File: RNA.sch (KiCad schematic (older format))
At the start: 89 parts, among them J1 USB_B_Micro, J2 AudioJack4, J3 Conn_01x06, J4 AudioJack4, SW1 SW_SPST, SW11 SW_Push_45deg, SW12 SW_Push_45deg, SW13 SW_Push_45deg, SW14 SW_Push_45deg, SW15 SW_Push_45deg, SW16 SW_Push_45deg, SW2 SW_Push, SW21 SW_Push_45deg, SW22 SW_Push_45deg, SW23 SW_Push_45deg, SW24 SW_Push_45deg, SW25 SW_Push_45deg, SW26 SW_Push_45deg, SW31 SW_Push_45deg, SW32 SW_Push_45deg, SW33 SW_Push_45deg, SW34 SW_Push_45deg, SW35 SW_Push_45deg, SW36 SW_Push_45deg, SW41 SW_Push_45deg, SW42 SW_Push_45deg, SW43 SW_Push_45deg, SW44 SW_Push_45deg, SW45 SW_Push_45deg, SW46 SW_Push_45deg, SW47 SW_Push_45deg, SW51 SW_Push_45deg, SW52 SW_Push_45deg, SW53 SW_Push_45deg, SW54 SW_Push_45deg, SW55 SW_Push_45deg, SW56 SW_Push_45deg, SW57 SW_Push_45deg, U1 STM32F072C8Tx, U2 PRTR5V0U2X, U3 MCP1703A-3302_SOT23

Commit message: ready to alpha
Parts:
- removed R4: 39k, Resistor_SMD:R_0603_1608Metric, symbol Device:R_Small
- removed R7: 68k, Resistor_SMD:R_0603_1608Metric, symbol Device:R_Small
- added C9: C_Small, Capacitor_SMD:C_0603_1608Metric, symbol Device:C_Small
- added U5: CAT24M01W, Package_SO:SOIC-8_3.9x4.9mm_P1.27mm, symbol Memory_EEPROM:CAT24M01W
- C7: value C_Small -> 100u
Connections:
- net GND: now also C9.2, U5.2 (A1), U5.3 (A2), U5.4 (GND), U5.7 (WP)
- net SCL1: now also U5.6 (SCL)
- net SDA1: now also U5.5 (SDA)
- net SWO: now also J3.6 (Pin_6)
- net VDD: now also C9.1, U5.8 (VCC)
- no-connect marks 3 -> 2
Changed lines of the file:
@@
 Wire Wire Line
 	1850 5400 1850 5350
-NoConn ~ 8400 1150
 $Comp
 L Device:C_Small C7
@@
 P 4550 1450
 F 0 "C7" H 4642 1496 50  0000 L CNN
-F 1 "C_Small" H 4642 1405 50  0000 L CNN
+F 1 "100u" H 4642 1405 50  0000 L CNN
 F 2 "Capacitor_SMD:C_0603_1608Metric" H 4550 1450 50  0001 C CNN
 F 3 "~" H 4550 1450 50  0001 C CNN
@@
 Wire Wire Line
 	1750 5950 2300 5950
-$Comp
-L power:VBUS #PWR0107
-U 1 1 5CDEAD02
-P 9650 800
-F 0 "#PWR0107" H 9650 650 50  0001 C CNN
-F 1 "VBUS" H 9665 973 50  0000 C CNN
-F 2 "" H 9650 800 50  0001 C CNN
-F 3 "" H 9650 800 50  0001 C CNN
-	1    9650 800
-	1    0    0    -1
-$EndComp
-$Comp
-L power:GND #PWR0120
-U 1 1 5CDEAE65
-P 9650 1700
-F 0 "#PWR0120" H 9650 1450 50  0001 C CNN
-F 1 "GND" H 9655 1527 50  0000 C CNN
-F 2 "" H 9650 1700 50  0001 C CNN
-F 3 "" H 9650 1700 50  0001 C CNN
-	1    9650 1700
-	1    0    0    -1
-$EndComp
-$Comp
-L Device:R_Small R4
-U 1 1 5CDEAFCF
-P 9650 1050
-F 0 "R4" H 9709 1096 50  0000 L CNN
-F 1 "39k" H 9709 1005 50  0000 L CNN
-F 2 "Resistor_SMD:R_0603_1608Metric" H 9650 1050 50  0001 C CNN
-F 3 "~" H 9650 1050 50  0001 C CNN
-	1    9650 1050
-	1    0    0    -1
-$EndComp
-$Comp
-L Device:R_Small R7
-U 1 1 5CDEB0FC
-P 9650 1500
-F 0 "R7" H 9709 1546 50  0000 L CNN
-F 1 "68k" H 9709 1455 50  0000 L CNN
-F 2 "Resistor_SMD:R_0603_1608Metric" H 9650 1500 50  0001 C CNN
-F 3 "~" H 9650 1500 50  0001 C CNN
-	1    9650 1500
-	1    0    0    -1
-$EndComp
-Wire Wire Line
-	9650 950  9650 800
-Wire Wire Line
-	9650 1400 9650 1250
-Wire Wire Line
-	9650 1700 9650 1600
-Text GLabel 9850 1250 2    50   Output ~ 0
-VBUS_SENSE
-Wire Wire Line
-	9850 1250 9650 1250
-Connection ~ 9650 1250
-Wire Wire Line
-	9650 1250 9650 1150
 Connection ~ 4900 1750
 $Comp
@@
 F1 "RNA_Sub.sch" 50
 $EndSheet
+$Comp
+L Memory_EEPROM:CAT24M01W U5
+U 1 1 5D0A58A2
+P 10000 1350
+F 0 "U5" H 10000 1831 50  0000 C CNN
+F 1 "CAT24M01W" H 10000 1740 50  0000 C CNN
+F 2 "Package_SO:SOIC-8_3.9x4.9mm_P1.27mm" H 10850 1100 50  0001 C CNN
+F 3 "https://www.onsemi.com/pub/Collateral/CAT24M01-D.PDF" H 10000 1350 50  0001 C CNN
+	1    10000 1350
+	1    0    0    -1
+$EndComp
+Wire Wire Line
+	8650 1150 8400 1150
+$Comp
+L power:GND #PWR0107
+U 1 1 5D0C7181
+P 10000 1850
+F 0 "#PWR0107" H 10000 1600 50  0001 C CNN
+F 1 "GND" H 10005 1677 50  0000 C CNN
+F 2 "" H 10000 1850 50  0001 C CNN
+F 3 "" H 10000 1850 50  0001 C CNN
+	1    10000 1850
+	1    0    0    -1
+$EndComp
+Wire Wire Line
+	10000 1650 10000 1750
+Wire Wire Line
+	9600 1450 9600 1750
+Wire Wire Line
+	9600 1750 10000 1750
+Connection ~ 10000 1750
+Wire Wire Line
+	10000 1750 10000 1850
+Wire Wire Line
+	9600 1350 9600 1450
+Connection ~ 9600 1450
+Text GLabel 10550 1250 2    50   Input ~ 0
+SDA1
+Text GLabel 10550 1350 2    50   Input ~ 0
+SCL1
+$Comp
+L power:VDD #PWR0120
+U 1 1 5D120387
+P 10000 900
+F 0 "#PWR0120" H 10000 750 50  0001 C CNN
+F 1 "VDD" H 10017 1073 50  0000 C CNN
+F 2 "" H 10000 900 50  0001 C CNN
+F 3 "" H 10000 900 50  0001 C CNN
+	1    10000 900
+	1    0    0    -1
+$EndComp
+Wire Wire Line
+	10000 900  10000 950
+Wire Wire Line
+	10400 1250 10550 1250
+Wire Wire Line
+	10550 1350 10400 1350
+$Comp
+L Device:C_Small C9
+U 1 1 5D17A0FE
+P 9600 1100
+F 0 "C9" H 9692 1146 50  0000 L CNN
+F 1 "C_Small" H 9692 1055 50  0000 L CNN
+F 2 "Capacitor_SMD:C_0603_1608Metric" H 9600 1100 50  0001 C CNN
+F 3 "~" H 9600 1100 50  0001 C CNN
+	1    9600 1100
+	1    0    0    -1
+$EndComp
+Wire Wire Line
+	9600 1000 9600 950
+Wire Wire Line
+	9600 950  10000 950
+Connection ~ 10000 950
+Wire Wire Line
+	10000 950  10000 1050
+Wire Wire Line
+	9600 1200 9600 1350
+Connection ~ 9600 1350
+Wire Wire Line
+	10400 1450 10450 1450
+Wire Wire Line
+	10450 1450 10450 1750
+Wire Wire Line
+	10450 1750 10000 1750
 $EndSCHEMATC

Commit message: update annotation
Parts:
- renumbered C2 to C1, C3 to C2, C4 to C3, C6 to C4, C7 to C5, C1 to C6, C5 to C7, C9 to C8, D42 to D10, D52 to D11, D13 to D12, D23 to D13, D33 to D14, D43 to D15, D53 to D16, D14 to D17, D24 to D18, D34 to D19, D11 to D2, D44 to D20, D54 to D21, D15 to D22, D25 to D23, D35 to D24, D45 to D25, D55 to D26, D16 to D27, D26 to D28, D36 to D29, D21 to D3, D46 to D30, D56 to D31, D47 to D32, D57 to D33, D31 to D4, D41 to D5, D51 to D6, D12 to D7, D22 to D8, D32 to D9, J4 to J2, J2 to J3, J3 to J4, R3 to R1, R1 to R2, R2 to R3, R5 to R4, R6 to R5, SW32 to SW10, SW42 to SW11, SW52 to SW12, SW23 to SW14, SW33 to SW15, SW43 to SW16, SW53 to SW17, SW14 to SW18, SW24 to SW19, SW34 to SW20, SW44 to SW21, SW54 to SW22, SW15 to SW23, SW25 to SW24, SW35 to SW25, SW45 to SW26, SW55 to SW27, SW16 to SW28, SW26 to SW29, SW11 to SW3, SW36 to SW30, SW46 to SW31, SW56 to SW32, SW47 to SW33, SW57 to SW34, SW21 to SW4, SW31 to SW5, SW41 to SW6, SW51 to SW7, SW12 to SW8, SW22 to SW9, U5 to U4

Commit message: modify module
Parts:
- C8: value C_Small -> 100n
- D1: value D_Schottky_Small -> B5817WS
- D10, D11, D12, D13, D14, D15, D16, D17, D18, D19, D2, D20, D21, D22, D23, D24, D25, D26, D27, D28, D29, D3, D30, D31, D32, D33, D4, D5, D6, D7, D8, D9: value D_Small -> 1N4148W
- J2: value AudioJack4 -> SM04B-SRSS-TB(LF)(SN)
- R2, R3, R4, R5: value R_Small -> 2.2k
- SW10, SW11, SW12, SW13, SW14, SW15, SW16, SW17, SW18, SW19, SW20, SW21, SW22, SW23, SW24, SW25, SW26, SW27, SW28, SW29, SW3, SW30, SW31, SW32, SW33, SW34, SW4, SW5, SW6, SW7, SW8, SW9: value SW_Push_45deg -> CPG135001S30

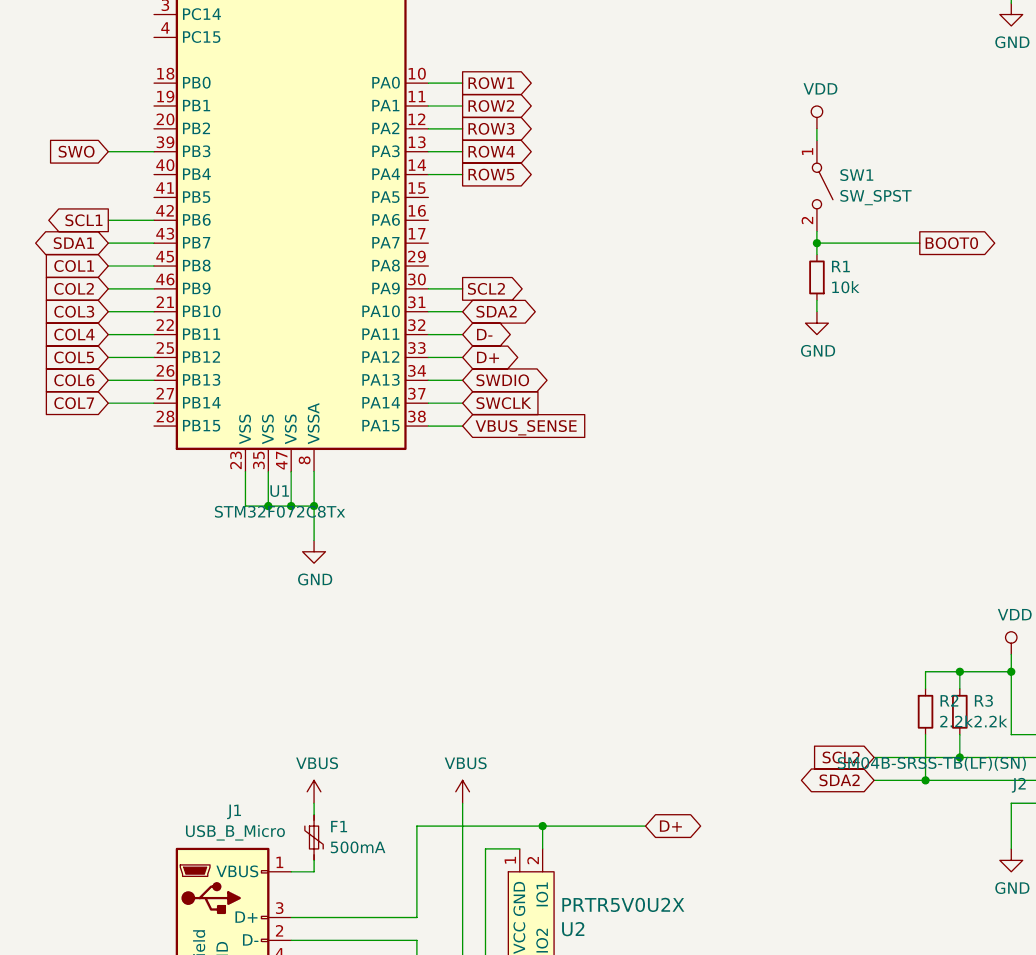
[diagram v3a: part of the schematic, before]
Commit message: Move conflicted I2C1 to I2C3
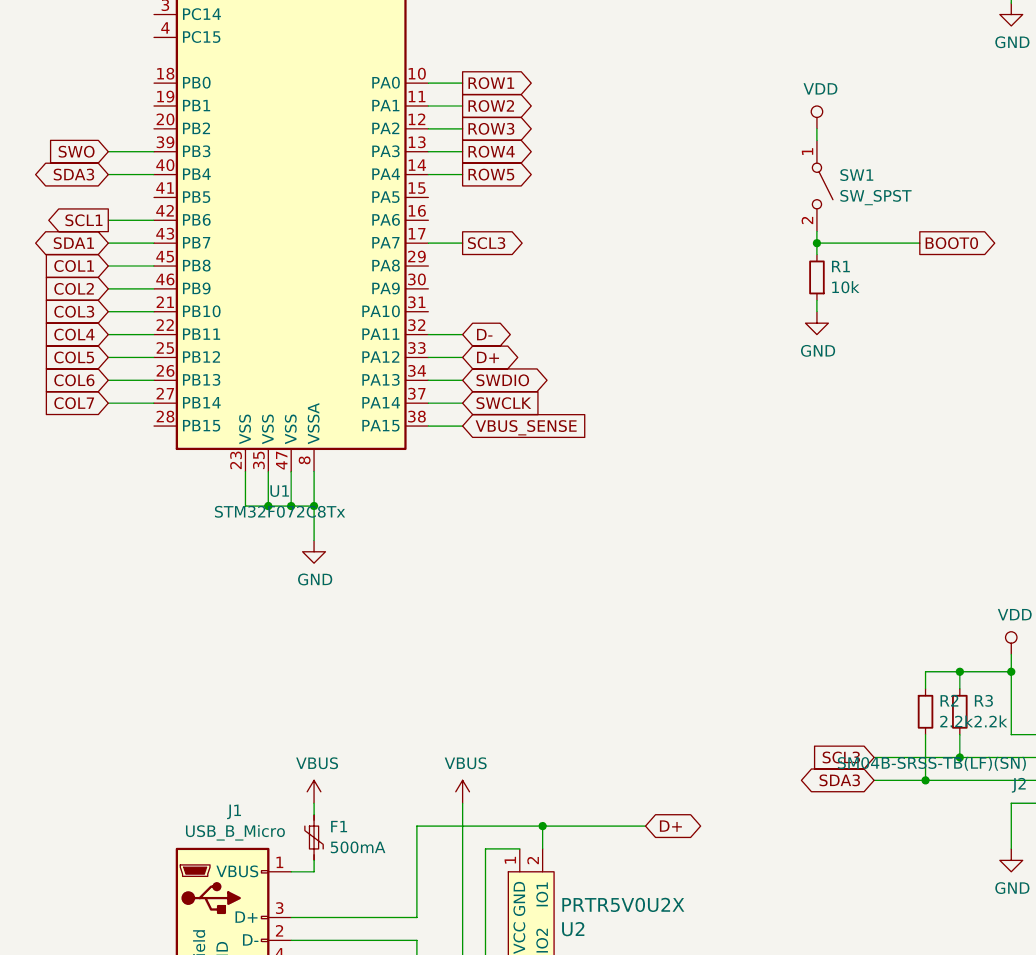
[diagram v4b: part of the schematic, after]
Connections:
- net SCL3: now reaches U1.17 (PA7)
- net SCL3: now also J2.2 (Pin_2), R3.2
- net SDA3: now reaches U1.40 (PB4)
- net SDA3: now also J2.3 (Pin_3), R2.2
- removed net SCL2: J2.2 (Pin_2), R3.2, U1.30 (PA9)
- removed net SDA2: J2.3 (Pin_3), R2.2, U1.31 (PA10)
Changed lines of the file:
@@
 Text GLabel 2500 3400 2    50   BiDi ~ 0
 D+
-Text GLabel 2500 3200 2    50   BiDi ~ 0
-SDA2
-Text GLabel 2500 3100 2    50   Output ~ 0
-SCL2
+Text GLabel 950  2600 0    50   BiDi ~ 0
+SDA3
+Text GLabel 2500 2900 2    50   Output ~ 0
+SCL3
 Text GLabel 950  2900 0    50   BiDi ~ 0
 SDA1
@@
 Connection ~ 5325 7000
 NoConn ~ 7300 1375
-Wire Wire Line
-	2350 3100 2500 3100
-Wire Wire Line
-	2350 3200 2500 3200
 Wire Wire Line
 	2350 3300 2500 3300
@@
 	4525 5250 5100 5250
 Text GLabel 4300 5150 0    50   Input ~ 0
-SCL2
+SCL3
 Text GLabel 4300 5250 0    50   BiDi ~ 0
-SDA2
+SDA3
 Connection ~ 4525 5250
 Connection ~ 4675 5150
@@
 Wire Wire Line
 	10450 1750 10000 1750
+Wire Wire Line
+	2350 2900 2500 2900
+Wire Wire Line
+	950  2600 1150 2600
 $EndSCHEMATC

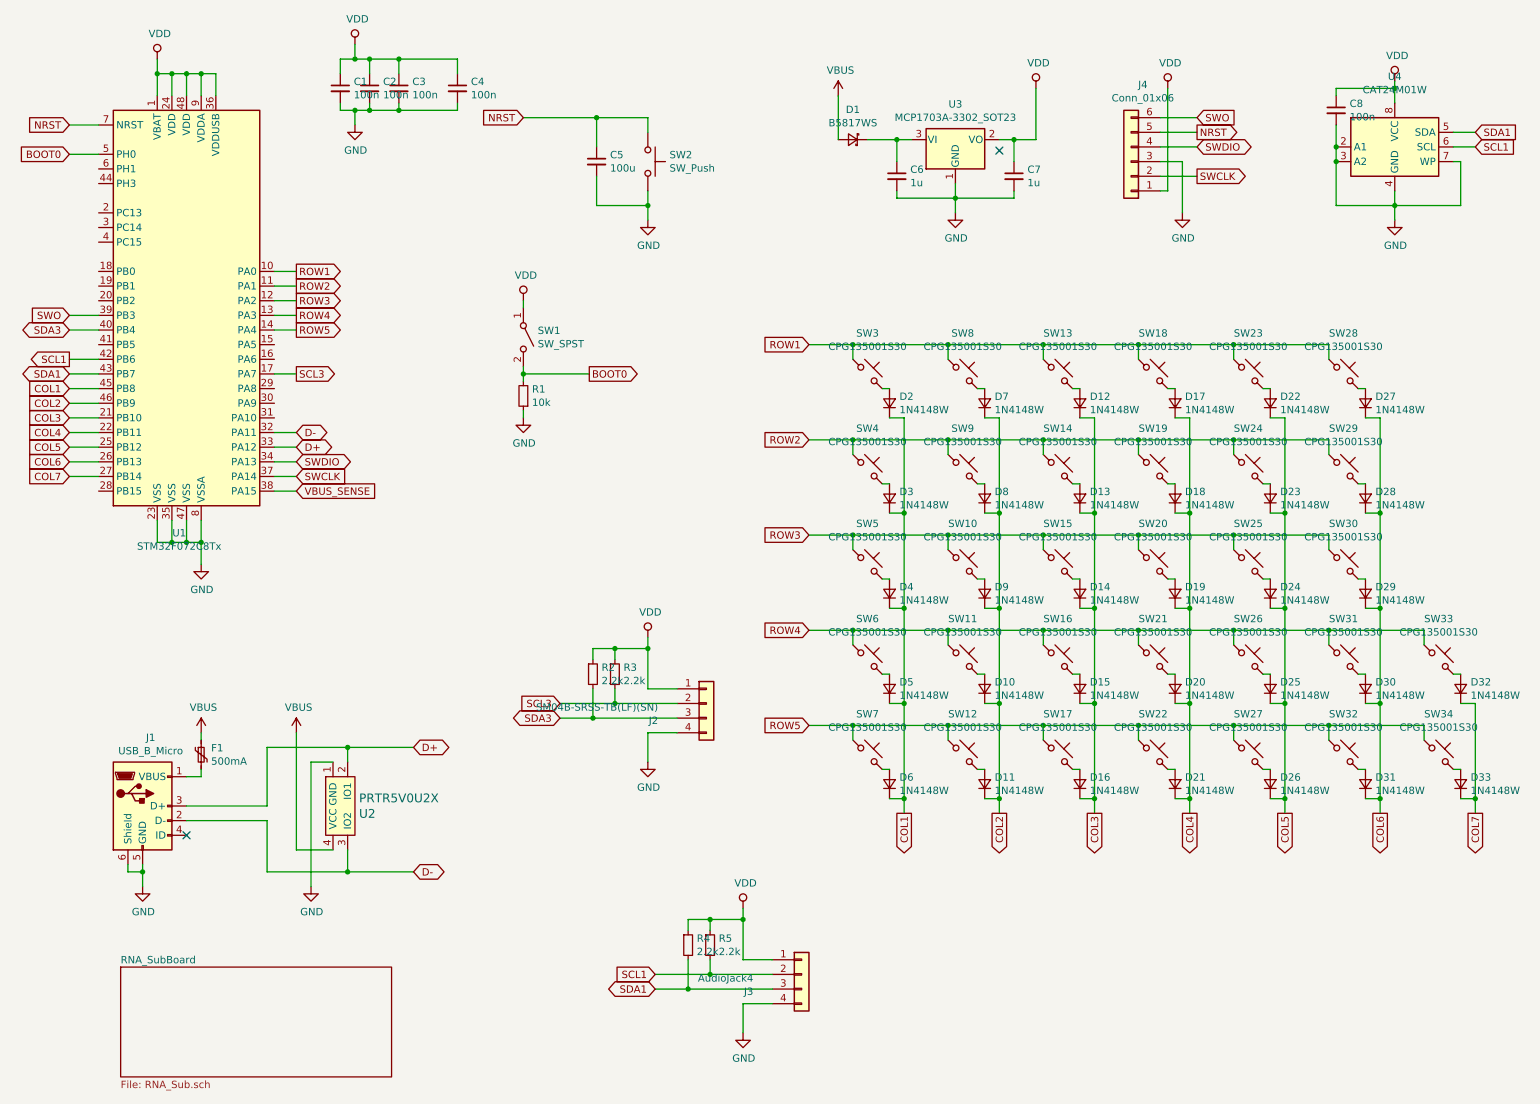
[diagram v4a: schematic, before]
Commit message: change EEPROM interface
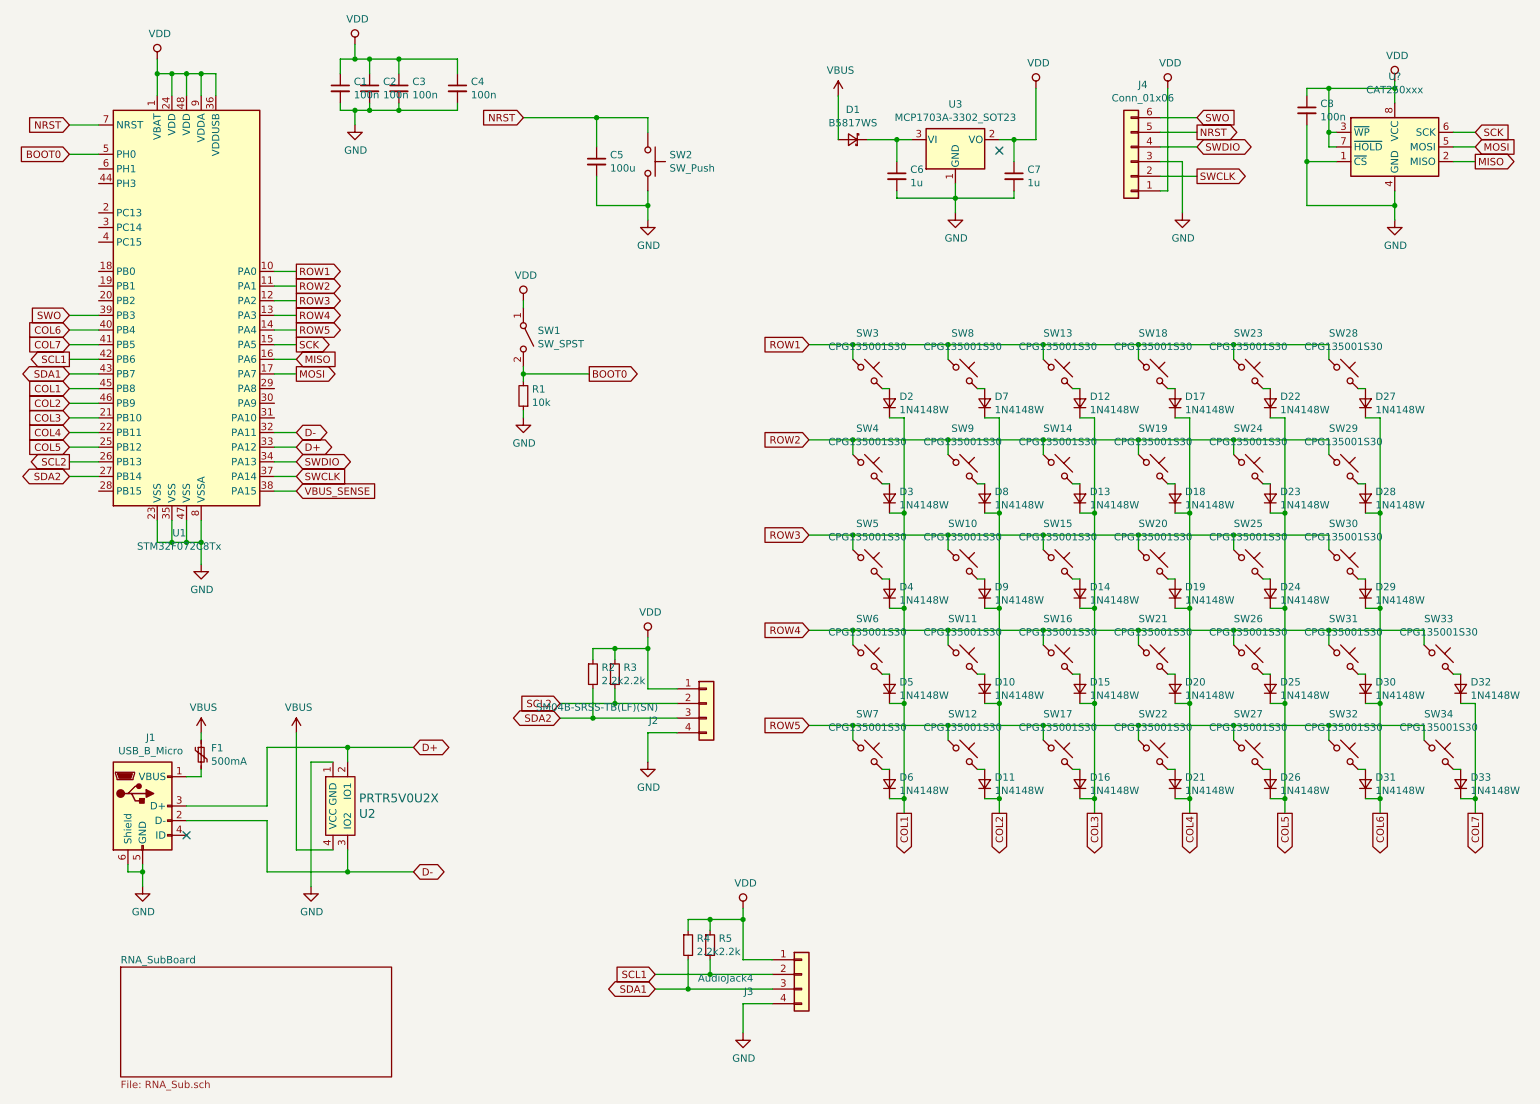
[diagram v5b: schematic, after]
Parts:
- removed U4: CAT24M01W, Package_SO:SOIC-8_3.9x4.9mm_P1.27mm, symbol Memory_EEPROM:CAT24M01W
- added U?: CAT250xxx, symbol Memory_EEPROM:CAT250xxx
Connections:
- net COL6: now also U1.40 (PB4); no longer U1.26 (PB13)
- net COL7: now also U1.41 (PB5); no longer U1.27 (PB14)
- net GND: now also U?.1 (~CS), U?.4 (GND)
- net VDD: now also U?.3 (~WP), U?.7 (~HOLD), U?.8 (VCC)
- net SCK: now reaches U1.15 (PA5)
- net SCK: now also U?.6 (SCK)
- net MISO: now reaches U1.16 (PA6)
- net MISO: now also U?.2 (MISO)
- net SCL3 renamed SCL2
- net SCL2: now also U1.26 (PB13); no longer U1.17 (PA7)
- net SDA3 renamed SDA2
- net SDA2: now also U1.27 (PB14); no longer U1.40 (PB4)
- new net MOSI: U1.17 (PA7), U?.5 (MOSI)
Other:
- moved on the sheet: C8
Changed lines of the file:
@@
 Text GLabel 2500 3400 2    50   BiDi ~ 0
 D+
-Text GLabel 950  2600 0    50   BiDi ~ 0
-SDA3
 Text GLabel 2500 2900 2    50   Output ~ 0
-SCL3
+MOSI
 Text GLabel 950  2900 0    50   BiDi ~ 0
 SDA1
@@
 Text GLabel 950  3400 0    50   Input ~ 0
 COL5
-Text GLabel 950  3500 0    50   Input ~ 0
+Text GLabel 950  2600 0    50   Input ~ 0
 COL6
-Text GLabel 950  3600 0    50   Input ~ 0
+Text GLabel 950  2700 0    50   Input ~ 0
 COL7
 Wire Wire Line
-	950  3600 1150 3600
-Wire Wire Line
-	950  3500 1150 3500
+	950  2700 1150 2700
+Wire Wire Line
+	950  2600 1150 2600
 Wire Wire Line
 	950  3400 1150 3400
@@
 	4525 5250 5100 5250
 Text GLabel 4300 5150 0    50   Input ~ 0
-SCL3
+SCL2
 Text GLabel 4300 5250 0    50   BiDi ~ 0
-SDA3
+SDA2
 Connection ~ 4525 5250
 Connection ~ 4675 5150
@@
 F1 "RNA_Sub.sch" 50
 $EndSheet
-$Comp
-L Memory_EEPROM:CAT24M01W U4
-U 1 1 5D0A58A2
-P 10000 1350
-F 0 "U4" H 10000 1831 50  0000 C CNN
-F 1 "CAT24M01W" H 10000 1740 50  0000 C CNN
-F 2 "Package_SO:SOIC-8_3.9x4.9mm_P1.27mm" H 10850 1100 50  0001 C CNN
-F 3 "https://www.onsemi.com/pub/Collateral/CAT24M01-D.PDF" H 10000 1350 50  0001 C CNN
-	1    10000 1350
-	1    0    0    -1
-$EndComp
 Wire Wire Line
 	8650 1150 8400 1150
@@
 Wire Wire Line
 	10000 1650 10000 1750
-Wire Wire Line
-	9600 1450 9600 1750
-Wire Wire Line
-	9600 1750 10000 1750
 Connection ~ 10000 1750
 Wire Wire Line
 	10000 1750 10000 1850
-Wire Wire Line
-	9600 1350 9600 1450
-Connection ~ 9600 1450
 Text GLabel 10550 1250 2    50   Input ~ 0
-SDA1
+SCK
 Text GLabel 10550 1350 2    50   Input ~ 0
-SCL1
+MOSI
 $Comp
 L power:VDD #PWR0122
@@
 L Device:C_Small C8
 U 1 1 5D17A0FE
-P 9600 1100
-F 0 "C8" H 9692 1146 50  0000 L CNN
-F 1 "100n" H 9692 1055 50  0000 L CNN
-F 2 "Capacitor_SMD:C_0603_1608Metric" H 9600 1100 50  0001 C CNN
-F 3 "~" H 9600 1100 50  0001 C CNN
-	1    9600 1100
-	1    0    0    -1
-$EndComp
-Wire Wire Line
-	9600 1000 9600 950
-Wire Wire Line
-	9600 950  10000 950
+P 9400 1100
+F 0 "C8" H 9492 1146 50  0000 L CNN
+F 1 "100n" H 9492 1055 50  0000 L CNN
+F 2 "Capacitor_SMD:C_0603_1608Metric" H 9400 1100 50  0001 C CNN
+F 3 "~" H 9400 1100 50  0001 C CNN
+	1    9400 1100
+	1    0    0    -1
+$EndComp
 Connection ~ 10000 950
 Wire Wire Line
 	10000 950  10000 1050
 Wire Wire Line
-	9600 1200 9600 1350
-Connection ~ 9600 1350
-Wire Wire Line
-	10400 1450 10450 1450
-Wire Wire Line
-	10450 1450 10450 1750
-Wire Wire Line
-	10450 1750 10000 1750
-Wire Wire Line
 	2350 2900 2500 2900
-Wire Wire Line
-	950  2600 1150 2600
+$Comp
+L Memory_EEPROM:CAT250xxx U?
+U 1 1 5D17739A
+P 10000 1350
+F 0 "U?" H 10000 1831 50  0000 C CNN
+F 1 "CAT250xxx" H 10000 1740 50  0000 C CNN
+F 2 "" H 10000 1350 50  0001 C CNN
+F 3 "http://www.onsemi.com/PowerSolutions/product.do?id=CAT25040" H 10000 1350 50  0001 C CNN
+	1    10000 1350
+	1    0    0    -1
+$EndComp
+Text GLabel 10550 1450 2    50   Output ~ 0
+MISO
+Wire Wire Line
+	10400 1450 10550 1450
+Wire Wire Line
+	9400 950  9400 1000
+Wire Wire Line
+	9400 950  9550 950
+Wire Wire Line
+	9400 1750 10000 1750
+Wire Wire Line
+	9600 1450 9400 1450
+Connection ~ 9400 1450
+Wire Wire Line
+	9400 1450 9400 1750
+Text GLabel 2500 2700 2    50   Output ~ 0
+SCK
+Text GLabel 2500 2800 2    50   Input ~ 0
+MISO
+Wire Wire Line
+	2350 2700 2500 2700
+Wire Wire Line
+	2350 2800 2500 2800
+Text GLabel 950  3500 0    50   Output ~ 0
+SCL2
+Text GLabel 950  3600 0    50   BiDi ~ 0
+SDA2
+Wire Wire Line
+	950  3500 1150 3500
+Wire Wire Line
+	950  3600 1150 3600
+Wire Wire Line
+	9400 1200 9400 1450
+Wire Wire Line
+	9600 1250 9550 1250
+Wire Wire Line
+	9550 1250 9550 950
+Connection ~ 9550 950
+Wire Wire Line
+	9550 950  10000 950
+Wire Wire Line
+	9550 1350 9550 1250
+Wire Wire Line
+	9550 1350 9600 1350
+Connection ~ 9550 1250
 $EndSCHEMATC
